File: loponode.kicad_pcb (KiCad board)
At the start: 2 copper layers, 24 parts, among them J1 DEBUG, J2 POWER_IN, J3 DBG_UART, J4 Conn_01x16, U1 TPS61322, U2 STM32L073CBTx, U3 NRF24L01+, Y1 Crystal

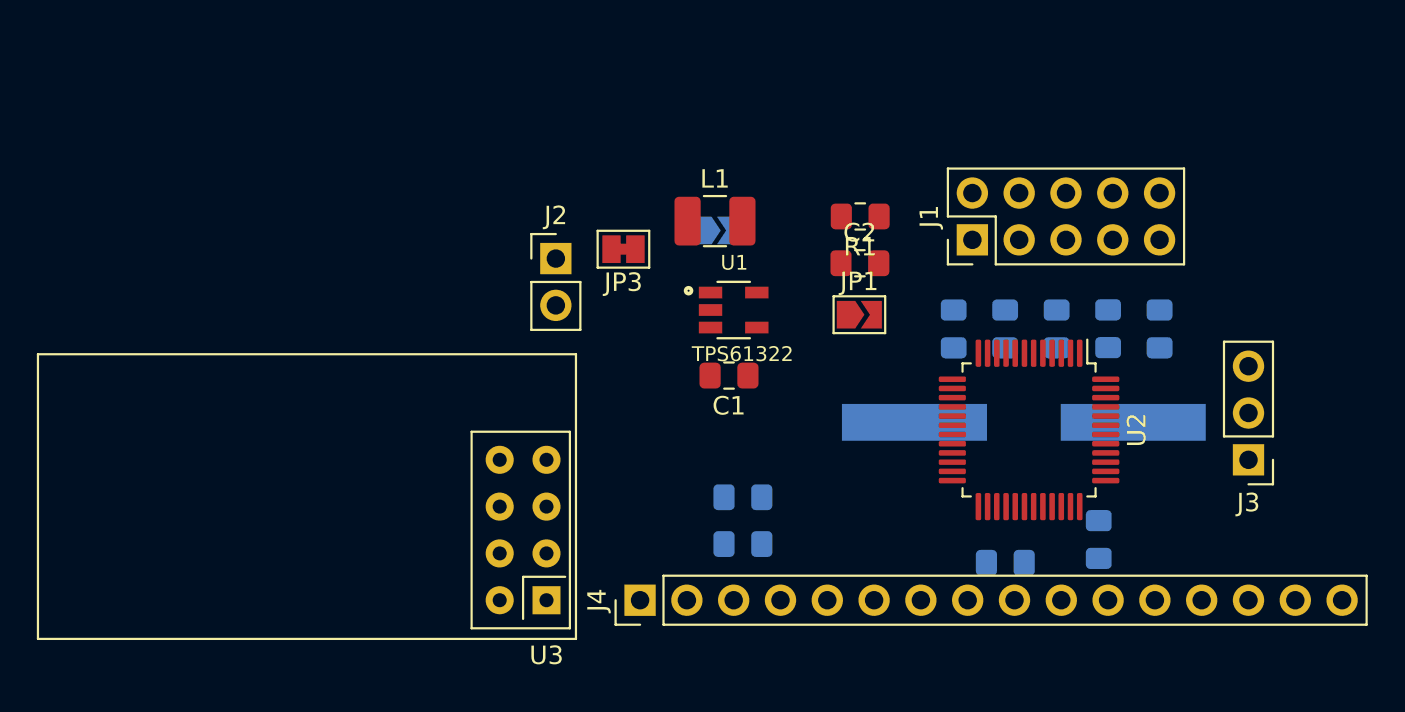
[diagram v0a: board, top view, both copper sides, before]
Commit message: add some wires
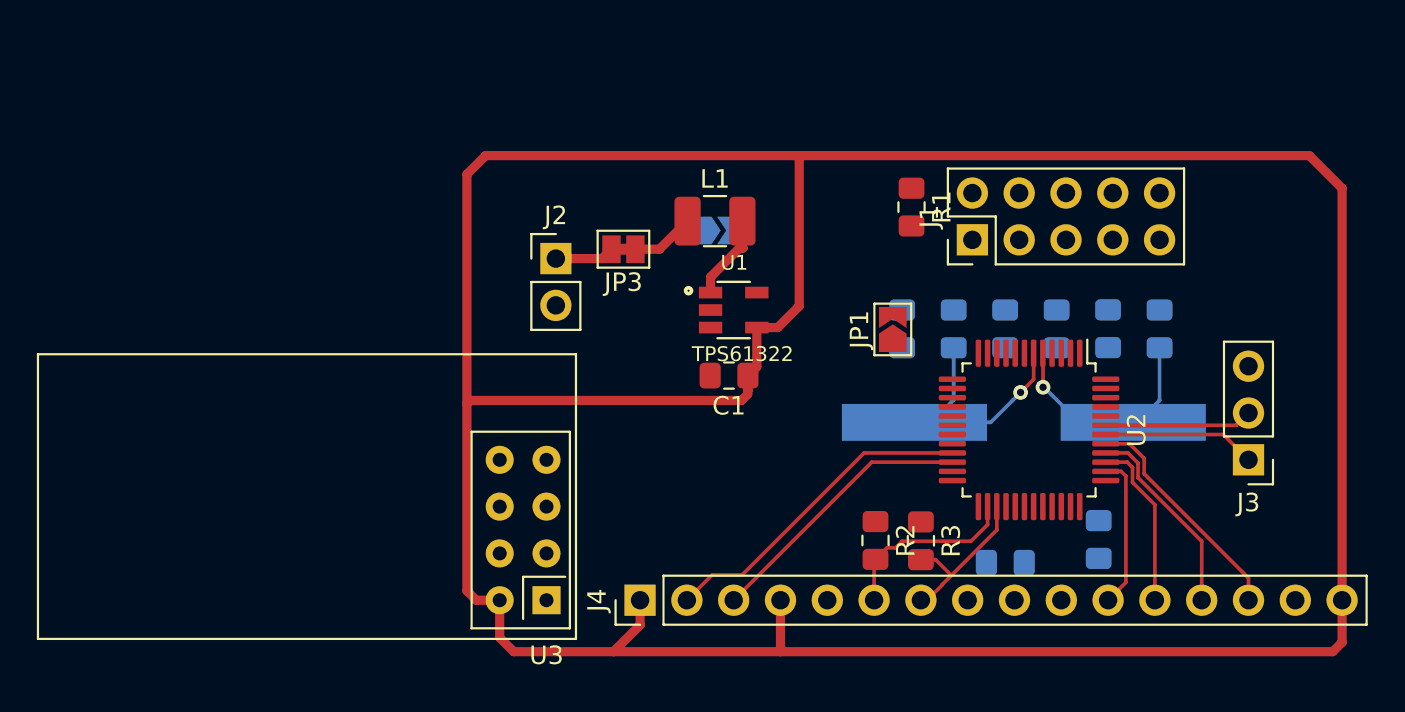
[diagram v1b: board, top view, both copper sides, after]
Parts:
- C2: moved to B.Cu
- R2, R3: moved to F.Cu
- moved R3 9.95 mm to (137.2, 141.6), turned to 270 degrees
- moved R2 7.20 mm to (134.7, 141.5), turned to 270 degrees
- moved C2 4.24 mm to (136.1, 130.1), turned to 90 degrees
- moved R1 2.83 mm to (136.7, 123.4), turned to 270 degrees
- moved JP1 1.98 mm to (135.6, 130.1), turned to 90 degrees
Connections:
- J4 pad 1: +3V3 -> GND
- J4 pad 11: GPIO_PB3 -> GPIO_PA15
- J4 pad 12: GPIO_PB4 -> GPIO_PB3
- J4 pad 13: GPIO_PB5 -> GPIO_PB4
- J4 pad 14: GPIO_PA15 -> GPIO_PB5
- J4 pad 2: GND -> UART_RX
- J4 pad 3: SCL -> UART_TX
- J4 pad 4: SDA -> +3V3
- J4 pad 6: UART_TX -> SCL
- J4 pad 7: UART_RX -> SDA
- U2 pad 26: Net-(U2-Pad26) -> SCL
- U2 pad 27: Net-(U2-Pad27) -> SDA
- U2 pad 45: SCL -> Net-(U2-Pad45)
- U2 pad 46: SDA -> Net-(U2-Pad46)
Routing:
- net +3V3: track 0.00 -> 182.6 mm
- net UART_RX: track 0.00 -> 17.7 mm
- net UART_TX: track 0.00 -> 15.0 mm
- net Net-(C9-Pad1): track 0.00 -> 14.3 mm, vias 0 -> 1
- net GPIO_PB5: track 0.00 -> 12.5 mm
- net Net-(C8-Pad1): track 0.00 -> 12.3 mm, vias 0 -> 1
- net GPIO_PB4: track 0.00 -> 10.9 mm
- net SCL: track 0.00 -> 10.1 mm
- net GPIO_PB3: track 0.00 -> 9.28 mm
- net SDA: track 0.00 -> 8.99 mm
- net GPIO_PA15: track 0.00 -> 8.34 mm
- net DBG_TX: track 0.00 -> 8.32 mm
- net DBG_RX: track 0.00 -> 8.02 mm
- net Net-(L1-Pad2): track 0.00 -> 4.72 mm
- net +BATT: track 0.00 -> 3.46 mm
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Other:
- net class Default: clearance 0.2 -> 0.1; trace_width 0.25 -> 0.2
- net class Power added: clearance 0.2, trace_width 0.5, via_dia 1, via_drill 0.6
- rule trace_clearance: 0.2 -> 0.1

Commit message: many optimizations; LAYOUT!
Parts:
- added REF**: OSHW-Logo_5.7x6mm_SilkScreen, Symbol:OSHW-Logo_5.7x6mm_SilkScreen, F.Cu at (132.9, 117.2)
- J4: value Conn_01x16 -> Conn_01x14; footprint Connector_PinHeader_2.54mm:PinHeader_1x16_P2.54mm_Vertical -> Connector_PinHeader_2.54mm:PinHeader_1x14_P2.54mm_Vertical
- R1, R2, R3: moved to B.Cu
- Y1: value Crystal -> 8MHz; footprint Crystal:Crystal_SMD_HC49-SD_HandSoldering -> Crystal:Crystal_SMD_EuroQuartz_MQ-4Pin_7.0x5.0mm_HandSoldering
- moved C8 19.3 mm to (131.1, 133.1), turned to 180 degrees
- moved Y1 15.7 mm to (127.3, 137.8)
- moved C9 15.4 mm to (123.9, 133.1), turned to 180 degrees
- moved JP2 6.71 mm to (132.7, 124.6)
- moved J3 3.97 mm to (151.6, 139.4)
- moved C6 2.92 mm to (144.4, 141.5), turned to 270 degrees
- moved J1 1.78 mm to (140.0, 127.0)
- moved R1 1.25 mm to (136.9, 124.7)
- moved C5 0.94 mm to (146.7, 130.7)
- moved C3 0.93 mm to (141.1, 130.7)
- moved C7 0.93 mm to (143.9, 130.7)
- moved C2 0.93 mm to (135.5, 130.7)
- moved JP1 0.78 mm to (135.0, 130.5)
- moved L1 0.26 mm to (125.9, 124.5)
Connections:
- J4 pad 10: DBG_RX -> GPIO_PB3
- J4 pad 11: GPIO_PA15 -> GPIO_PB4
- J4 pad 12: GPIO_PB3 -> GPIO_PB5
- J4 pad 13: GPIO_PB4 -> GND
- J4 pad 14: GPIO_PB5 -> +3V3
- J4 pad 9: DBG_TX -> GPIO_PA15
- U2 pad 10: Net-(JP2-Pad2) -> Net-(U2-Pad10)
- U2 pad 11: Net-(U2-Pad11) -> Net-(JP2-Pad2)
- U2 pad 20: Net-(U2-Pad20) -> /RF_CE
- U3 pad 3: Net-(U2-Pad32) -> /RF_CE
- U3 pad 8: Net-(U2-Pad33) -> Net-(U2-Pad10)
- Y1 pad 2: Net-(C9-Pad1) -> GND
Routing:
- net GND: track 0.00 -> 147.6 mm, vias 0 -> 73
- net Net-(U2-Pad17): track 0.00 -> 33.8 mm, vias 0 -> 4
- net Net-(U2-Pad10): track 0.00 -> 33.3 mm
- net +3V3: track 182.6 -> 214.4 mm, vias 0 -> 6
- net Net-(U2-Pad14): track 0.00 -> 31.3 mm, vias 0 -> 2
- net /SWCLK: track 0.00 -> 26.6 mm, vias 0 -> 2
- net Net-(U2-Pad15): track 0.00 -> 26.0 mm, vias 0 -> 2
- net /RF_CE: track 0.00 -> 24.5 mm
- net Net-(U2-Pad16): track 0.00 -> 23.4 mm
- net /NRST: track 0.00 -> 22.3 mm, vias 0 -> 1
- net /SWDIO: track 0.00 -> 18.8 mm, vias 0 -> 2
- net EXTINT: track 0.00 -> 16.9 mm
- net Net-(C9-Pad1): track 14.3 -> 26.0 mm
- net Net-(JP2-Pad2): track 0.00 -> 11.4 mm, vias 0 -> 3
- net +BATT: track 3.46 -> 13.8 mm, vias 0 -> 1
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- added copper zone on B.Cu, net GND
- added copper zone on F.Cu, net GND
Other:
- board outline added: 44.4 x 25.9 mm
- net class Default: via_dia 0.8 -> 0.6
- net class Power: clearance 0.2 -> 0.1; trace_width 0.5 -> 0.4; via_dia 1 -> 0.8
- board text added: "github.com/michz"
